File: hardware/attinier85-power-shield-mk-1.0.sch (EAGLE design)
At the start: 6 parts, among them Q1 2N7000, U1 ATTINIEST85_SHIELD

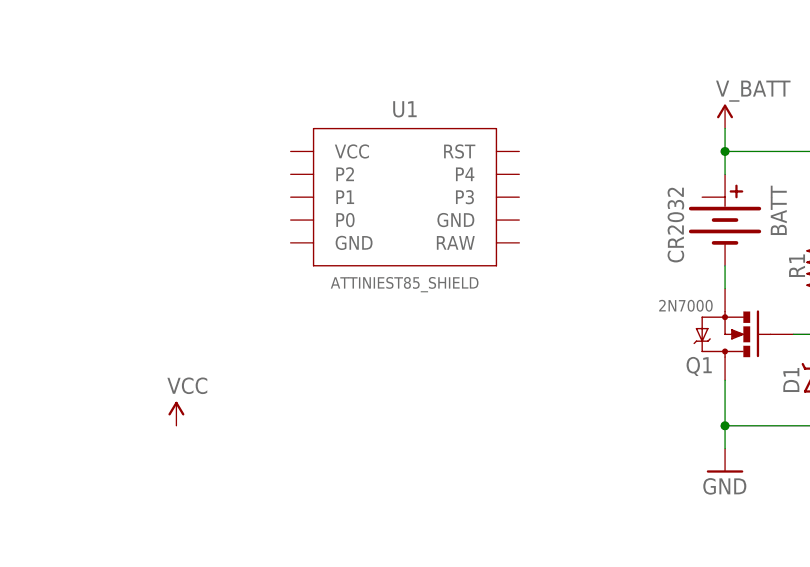
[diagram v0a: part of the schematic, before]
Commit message: renaming parts
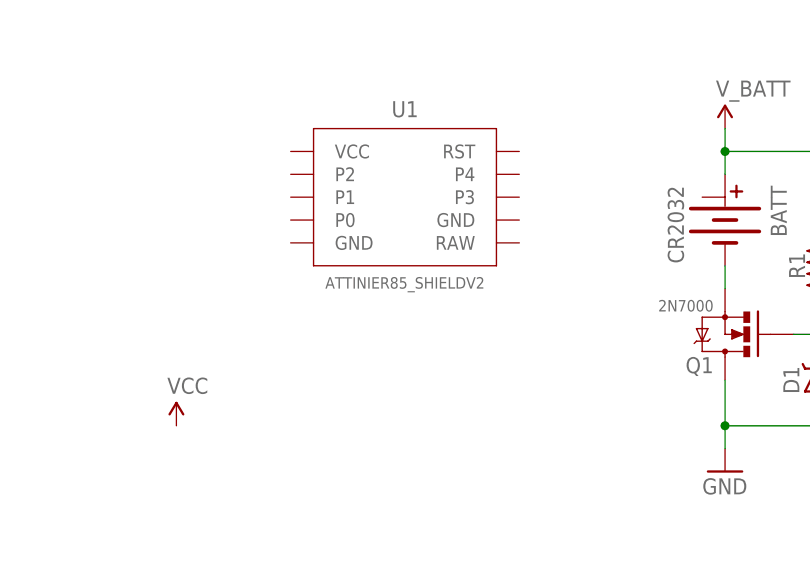
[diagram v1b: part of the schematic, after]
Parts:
- U1: value ATTINIEST85_SHIELD -> ATTINIER85_SHIELDV2; device A_butts:ATTINIEST85_SHIELD -> A_butts:ATTINIER85_SHIELDV2
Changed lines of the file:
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@@
 <grid distance="100" unitdist="mil" unit="mil" style="lines" multiple="1" display="yes" altdistance="2" altunitdist="mil" altunit="mil"/>
 <layers>
-<layer number="1" name="Top" color="4" fill="1" visible="yes" active="no"/>
-<layer number="16" name="Bottom" color="1" fill="1" visible="yes" active="no"/>
-<layer number="17" name="Pads" color="2" fill="1" visible="yes" active="no"/>
-<layer number="18" name="Vias" color="2" fill="1" visible="yes" active="no"/>
-<layer number="19" name="Unrouted" color="6" fill="1" visible="yes" active="no"/>
-<layer number="20" name="Dimension" color="15" fill="1" visible="yes" active="no"/>
-<layer number="21" name="tPlace" color="7" fill="1" visible="yes" active="no"/>
-<layer number="22" name="bPlace" color="7" fill="1" visible="yes" active="no"/>
-<layer number="23" name="tOrigins" color="15" fill="1" visible="yes" active="no"/>
-<layer number="24" name="bOrigins" color="15" fill="1" visible="yes" active="no"/>
-<layer number="25" name="tNames" color="7" fill="1" visible="yes" active="no"/>
-<layer number="26" name="bNames" color="7" fill="1" visible="yes" active="no"/>
-<layer number="27" name="tValues" color="7" fill="1" visible="yes" active="no"/>
-<layer number="28" name="bValues" color="7" fill="1" visible="yes" active="no"/>
+<layer number="1" name="Top" color="4" fill="1" visible="no" active="no"/>
+<layer number="16" name="Bottom" color="1" fill="1" visible="no" active="no"/>
+<layer number="17" name="Pads" color="2" fill="1" visible="no" active="no"/>
+<layer number="18" name="Vias" color="2" fill="1" visible="no" active="no"/>
+<layer number="19" name="Unrouted" color="6" fill="1" visible="no" active="no"/>
+<layer number="20" name="Dimension" color="15" fill="1" visible="no" active="no"/>
+<layer number="21" name="tPlace" color="7" fill="1" visible="no" active="no"/>
+<layer number="22" name="bPlace" color="7" fill="1" visible="no" active="no"/>
+<layer number="23" name="tOrigins" color="15" fill="1" visible="no" active="no"/>
+<layer number="24" name="bOrigins" color="15" fill="1" visible="no" active="no"/>
+<layer number="25" name="tNames" color="7" fill="1" visible="no" active="no"/>
+<layer number="26" name="bNames" color="7" fill="1" visible="no" active="no"/>
+<layer number="27" name="tValues" color="7" fill="1" visible="no" active="no"/>
+<layer number="28" name="bValues" color="7" fill="1" visible="no" active="no"/>
 <layer number="29" name="tStop" color="7" fill="3" visible="no" active="no"/>
 <layer number="30" name="bStop" color="7" fill="6" visible="no" active="no"/>
@@
 <layer number="35" name="tGlue" color="7" fill="4" visible="no" active="no"/>
 <layer number="36" name="bGlue" color="7" fill="5" visible="no" active="no"/>
-<layer number="37" name="tTest" color="7" fill="1" visible="yes" active="no"/>
-<layer number="38" name="bTest" color="7" fill="1" visible="yes" active="no"/>
+<layer number="37" name="tTest" color="7" fill="1" visible="no" active="no"/>
+<layer number="38" name="bTest" color="7" fill="1" visible="no" active="no"/>
 <layer number="39" name="tKeepout" color="4" fill="11" visible="no" active="no"/>
 <layer number="40" name="bKeepout" color="1" fill="11" visible="no" active="no"/>
@@
 <layer number="44" name="Drills" color="7" fill="1" visible="no" active="no"/>
 <layer number="45" name="Holes" color="7" fill="1" visible="no" active="no"/>
-<layer number="46" name="Milling" color="3" fill="1" visible="yes" active="no"/>
-<layer number="47" name="Measures" color="7" fill="1" visible="yes" active="no"/>
-<layer number="48" name="Document" color="7" fill="1" visible="yes" active="no"/>
-<layer number="49" name="Reference" color="7" fill="1" visible="yes" active="no"/>
-<layer number="50" name="dxf" color="7" fill="1" visible="yes" active="no"/>
-<layer number="51" name="tDocu" color="7" fill="1" visible="yes" active="no"/>
-<layer number="52" name="bDocu" color="7" fill="1" visible="yes" active="no"/>
-<layer number="53" name="tGND_GNDA" color="7" fill="9" visible="yes" active="no"/>
-<layer number="54" name="bGND_GNDA" color="1" fill="9" visible="yes" active="no"/>
-<layer number="56" name="wert" color="7" fill="1" visible="yes" active="no"/>
-<layer number="57" name="tCAD" color="7" fill="1" visible="yes" active="no"/>
+<layer number="46" name="Milling" color="3" fill="1" visible="no" active="no"/>
+<layer number="47" name="Measures" color="7" fill="1" visible="no" active="no"/>
+<layer number="48" name="Document" color="7" fill="1" visible="no" active="no"/>
+<layer number="49" name="Reference" color="7" fill="1" visible="no" active="no"/>
+<layer number="50" name="dxf" color="7" fill="1" visible="no" active="no"/>
+<layer number="51" name="tDocu" color="7" fill="1" visible="no" active="no"/>
+<layer number="52" name="bDocu" color="7" fill="1" visible="no" active="no"/>
+<layer number="53" name="tGND_GNDA" color="7" fill="9" visible="no" active="no"/>
+<layer number="54" name="bGND_GNDA" color="1" fill="9" visible="no" active="no"/>
+<layer number="56" name="wert" color="7" fill="1" visible="no" active="no"/>
+<layer number="57" name="tCAD" color="7" fill="1" visible="no" active="no"/>
 <layer number="90" name="Modules" color="5" fill="1" visible="yes" active="yes"/>
 <layer number="91" name="Nets" color="2" fill="1" visible="yes" active="yes"/>
@@
 <parts>
 <part name="FRAME1" library="A_butts" deviceset="FRAME-LETTER" device="NO_PACKAGE"/>
-<part name="U1" library="A_butts" deviceset="ATTINIEST85_SHIELD" device=""/>
+<part name="U1" library="A_butts" deviceset="ATTINIER85_SHIELD" device="V2"/>
 <part name="SUPPLY1" library="A_butts" deviceset="VCC" device=""/>
 <part name="SUPPLY2" library="A_butts" deviceset="V_BATT" device=""/>

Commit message: shedding useless version
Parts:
- removed BATT: CR2032, A_butts:BATTERY-COINCR2032_SMD
- removed Q1: 2N7000, A_butts:MOSFET-NCHANNEL2N7000-AMMO
- removed R1: 100k, A_butts:RESISTORPTH-AXIAL-7.62MM
- added D2: 1N5819, A_butts:DIODE-SCHOTTKYPTH-10.16MM
- added IC1: MC34063DIP, A_butts:MC34063DIP
- added L1: 100 unf, A_butts:INDUCTORAXIAL-PTH-10.16MM
- D1: value 10V -> 1N5819; device A_butts:DIODE-ZENER7.62MM-PTH -> A_butts:DIODE-SCHOTTKYPTH-10.16MM
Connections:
- removed net N$1: BATT.-, Q1.S
- removed net N$2: D1.C, Q1.G, R1.1
- removed net V_BATT: BATT.+, R1.2
- new net VCC: U1.VCC
- new net VIN: U1.RAW
- net GND: now also U1.GND@1, U1.GND@2; no longer D1.A, Q1.D
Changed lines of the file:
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@@
 <part name="SUPPLY2" library="A_butts" deviceset="V_BATT" device=""/>
 <part name="GND1" library="A_butts" deviceset="GND" device=""/>
-<part name="BATT" library="A_butts" deviceset="BATTERY-COIN" device="CR2032_SMD" value="CR2032"/>
-<part name="Q1" library="A_butts" deviceset="MOSFET-NCHANNEL" device="2N7000-AMMO" value="2N7000"/>
-<part name="D1" library="A_butts" deviceset="DIODE-ZENER" device="7.62MM-PTH" value="10V"/>
-<part name="R1" library="A_butts" deviceset="RESISTOR" device="PTH-AXIAL-7.62MM" value="100k"/>
+<part name="GND2" library="A_butts" deviceset="GND" device=""/>
+<part name="SUPPLY3" library="A_butts" deviceset="VIN" device=""/>
+<part name="IC1" library="A_butts" deviceset="MC34063" device="DIP"/>
+<part name="L1" library="A_butts" deviceset="INDUCTOR" device="AXIAL-PTH-10.16MM" value="100 unf"/>
+<part name="D1" library="A_butts" deviceset="DIODE-SCHOTTKY" device="PTH-10.16MM" value="1N5819"/>
+<part name="D2" library="A_butts" deviceset="DIODE-SCHOTTKY" device="PTH-10.16MM" value="1N5819"/>
 </parts>
 <sheets>
@@
 <instance part="FRAME1" gate="V" x="154.94" y="0"/>
 <instance part="U1" gate="G$1" x="63.5" y="73.66"/>
-<instance part="SUPPLY1" gate="G$1" x="38.1" y="48.26"/>
+<instance part="SUPPLY1" gate="G$1" x="48.26" y="81.28"/>
 <instance part="SUPPLY2" gate="G$1" x="99.06" y="81.28"/>
-<instance part="GND1" gate="1" x="99.06" y="43.18"/>
-<instance part="BATT" gate="G$1" x="99.06" y="71.12" rot="R270"/>
-<instance part="Q1" gate="G$1" x="99.06" y="58.42" rot="R180"/>
-<instance part="D1" gate="G$1" x="109.22" y="53.34" rot="R90"/>
-<instance part="R1" gate="G$1" x="109.22" y="66.04" rot="R90"/>
+<instance part="GND1" gate="1" x="83.82" y="73.66" rot="R90"/>
+<instance part="GND2" gate="1" x="48.26" y="63.5"/>
+<instance part="SUPPLY3" gate="G$1" x="81.28" y="66.04" rot="R270"/>
+<instance part="IC1" gate="G$1" x="149.86" y="91.44"/>
+<instance part="L1" gate="G$1" x="127" y="119.38"/>
+<instance part="D1" gate="G$1" x="99.06" y="114.3"/>
+<instance part="D2" gate="G$1" x="99.06" y="104.14"/>
 </instances>
 <busses>
@@
 <net name="GND" class="0">
 <segment>
-<pinref part="Q1" gate="G$1" pin="D"/>
+<pinref part="GND2" gate="1" pin="GND"/>
+<wire x1="48.26" y1="66.04" x2="48.26" y2="68.58" width="0.1524" layer="91"/>
+<pinref part="U1" gate="G$1" pin="GND@2"/>
+<wire x1="48.26" y1="68.58" x2="50.8" y2="68.58" width="0.1524" layer="91"/>
+</segment>
+<segment>
+<pinref part="U1" gate="G$1" pin="GND@1"/>
 <pinref part="GND1" gate="1" pin="GND"/>
-<wire x1="99.06" y1="45.72" x2="99.06" y2="48.26" width="0.1524" layer="91"/>
-<wire x1="99.06" y1="48.26" x2="99.06" y2="53.34" width="0.1524" layer="91"/>
-<wire x1="99.06" y1="48.26" x2="109.22" y2="48.26" width="0.1524" layer="91"/>
-<junction x="99.06" y="48.26"/>
-<pinref part="D1" gate="G$1" pin="A"/>
-<wire x1="109.22" y1="48.26" x2="109.22" y2="50.8" width="0.1524" layer="91"/>
+<wire x1="81.28" y1="73.66" x2="76.2" y2="71.12" width="0.1524" layer="91"/>
 </segment>
 </net>
-<net name="N$1" class="0">
+<net name="VCC" class="0">
 <segment>
-<pinref part="BATT" gate="G$1" pin="-"/>
-<pinref part="Q1" gate="G$1" pin="S"/>
-<wire x1="99.06" y1="63.5" x2="99.06" y2="66.04" width="0.1524" layer="91"/>
+<pinref part="SUPPLY1" gate="G$1" pin="VCC"/>
+<wire x1="48.26" y1="81.28" x2="48.26" y2="78.74" width="0.1524" layer="91"/>
+<pinref part="U1" gate="G$1" pin="VCC"/>
+<wire x1="48.26" y1="78.74" x2="50.8" y2="78.74" width="0.1524" layer="91"/>
 </segment>
 </net>
-<net name="N$2" class="0">
+<net name="VIN" class="0">
 <segment>
-<pinref part="Q1" gate="G$1" pin="G"/>
-<wire x1="106.68" y1="58.42" x2="109.22" y2="58.42" width="0.1524" layer="91"/>
-<pinref part="D1" gate="G$1" pin="C"/>
-<wire x1="109.22" y1="58.42" x2="109.22" y2="55.88" width="0.1524" layer="91"/>
-<pinref part="R1" gate="G$1" pin="1"/>
-<wire x1="109.22" y1="58.42" x2="109.22" y2="60.96" width="0.1524" layer="91"/>
-<junction x="109.22" y="58.42"/>
+<pinref part="U1" gate="G$1" pin="RAW"/>
+<pinref part="SUPPLY3" gate="G$1" pin="VIN"/>
+<wire x1="81.28" y1="66.04" x2="76.2" y2="68.58" width="0.1524" layer="91"/>
 </segment>
 </net>
-<net name="V_BATT" class="0">
-<segment>
-<pinref part="BATT" gate="G$1" pin="+"/>
-<wire x1="99.06" y1="76.2" x2="99.06" y2="78.74" width="0.1524" layer="91"/>
-<pinref part="R1" gate="G$1" pin="2"/>
-<wire x1="99.06" y1="78.74" x2="109.22" y2="78.74" width="0.1524" layer="91"/>
-<wire x1="109.22" y1="78.74" x2="109.22" y2="71.12" width="0.1524" layer="91"/>
-<pinref part="SUPPLY2" gate="G$1" pin="V_BATT"/>
-<wire x1="99.06" y1="78.74" x2="99.06" y2="81.28" width="0.1524" layer="91"/>
-<junction x="99.06" y="78.74"/>
-</segment>
-</net>

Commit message: wooo
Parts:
- removed D2: 1N5819, A_butts:DIODE-SCHOTTKYPTH-10.16MM
- added C1, C2, C3: 22uF, A_butts:CAPACITOR-POLARIZEDE2.5-6
- added C4: 10nF, A_butts:CAPACITOR-CERAMIC025-024X044
- added C5: 200pF, A_butts:CAPACITOR-CERAMIC025-024X044
- added L2: 22uH, A_butts:INDUCTORAXIAL-PTH-10.16MM
- added R1: 5k, A_butts:RESISTORPTH-AXIAL-6.35MM
- added R2: 12.76k, A_butts:RESISTORPTH-AXIAL-6.35MM
- added R3: 37.24k, A_butts:RESISTORPTH-AXIAL-6.35MM
- IC1: value MC34063DIP -> CS5171; device A_butts:MC34063DIP -> A_butts:CS5171/3SOIC-CS5171
- L1: value 100 unf -> 22uH
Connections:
- new net N$1: C4.2, R1.1
- new net N$3: C4.1, C5.1, IC1.COMP
- new net N$4: IC1.FB, R2.1, R3.1
- new net N$6: C2.+, L1.2
- new net N$7: C2.-, D1.A, L2.2
- net GND: now also C1.-, C3.-, C5.2, IC1.AGND, IC1.PGND, L2.1, R1.2, R2.2
- net VCC: now also C3.+, D1.C, R3.2
- net VIN: now also C1.+, IC1.VCC, L1.1
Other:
- moved on the sheet: D1, IC1, L1, U1
